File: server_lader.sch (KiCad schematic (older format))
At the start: 75 parts, among them IC1 ATMEGA168PA-A, IC2 DAC8560, P1 5V_Vbatt, P10 DISPLAY_STECKER, P11 on/off, P12 A_regulation_out, P2 DISPLAY_STECKER, P3 CONN_02X03, P4 I2C, P5 IP+, P6 IP-, P7 UART, P8 CONN_01X01, P9 Drehrad, U1 ACS758, U2 LTV-356T, U3 ADUM3441, U4 RD-0512D, U5 TPS7A4901, U6 OPA188, U7 LM4040, Y1 RESONATEUR

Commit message: bugfixes und Vormerkungen für nächsten Version
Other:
- note added: "Änderungen für nächste Version:\n-Kurzschlussbrücke für 5VRT und Power_GND vorsehen\n-abblockkondensatoren für Button vorsehen\n-alternative Bestückungsvariante mit anderem Stromsensor"
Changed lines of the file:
@@
 LIBS:contrib
 LIBS:valves
+LIBS:toni
 LIBS:server_lader-cache
 EELAYER 25 0
@@
 Text Notes 9200 4400 0    60   ~ 0
 RFB = 10k\nRG1 = 3,3k\nRG2 = 10k
+Text Notes 7850 5850 0    60   ~ 0
+Änderungen für nächste Version:\n-Kurzschlussbrücke für 5VRT und Power_GND vorsehen\n-abblockkondensatoren für Button vorsehen\n-alternative Bestückungsvariante mit anderem Stromsensor
 $EndSCHEMATC

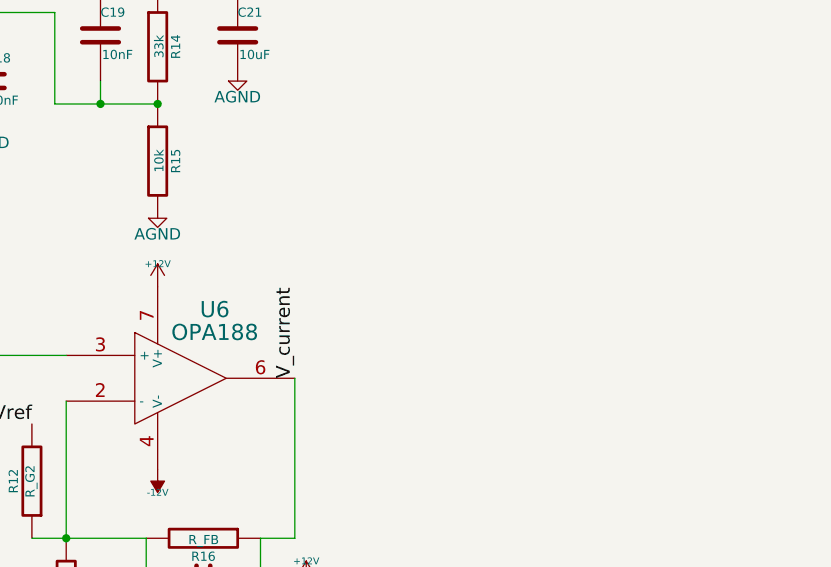
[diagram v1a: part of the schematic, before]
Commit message: Datenblätter und Schaltplananpassungen wegen neuem OPV im Ausgangszweig
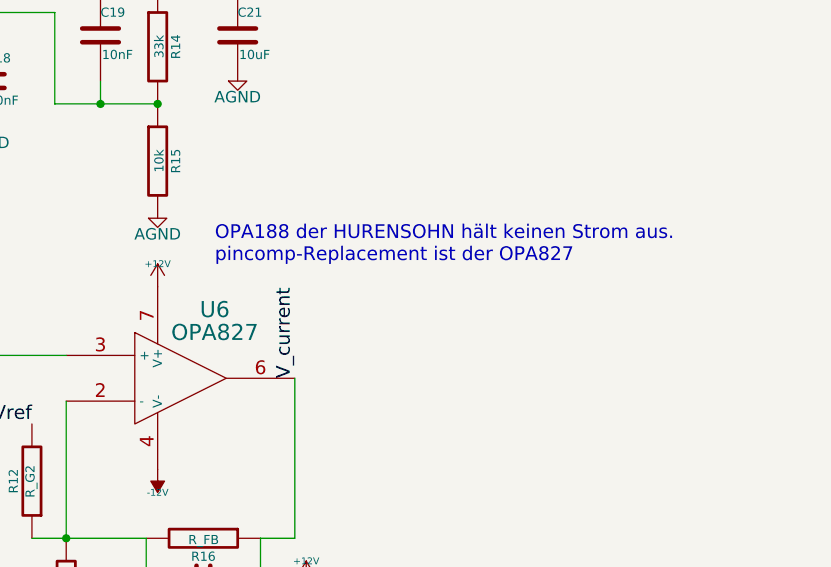
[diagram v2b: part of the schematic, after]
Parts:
- U6: value OPA188 -> OPA827
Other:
- note added: "OPA188 der HURENSOHN hält keinen Strom aus.\npincomp-Replacement ist der OPA827"
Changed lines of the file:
@@
 LIBS:contrib
 LIBS:valves
-LIBS:toni
 LIBS:server_lader-cache
 EELAYER 25 0
@@
 P 10450 3150
 F 0 "U6" H 10600 3450 70  0000 C CNN
-F 1 "OPA188" H 10600 3350 70  0000 C CNN
+F 1 "OPA827" H 10600 3350 70  0000 C CNN
 F 2 "SMD_Packages:SSOP-8" H 10450 3150 60  0001 C CNN
 F 3 "" H 10450 3150 60  0000 C CNN
@@
 Text Notes 7850 5850 0    60   ~ 0
 Änderungen für nächste Version:\n-Kurzschlussbrücke für 5VRT und Power_GND vorsehen\n-abblockkondensatoren für Button vorsehen\n-alternative Bestückungsvariante mit anderem Stromsensor
+Text Notes 10600 2650 0    60   ~ 0
+OPA188 der HURENSOHN hält keinen Strom aus.\npincomp-Replacement ist der OPA827
 $EndSCHEMATC

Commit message: kleine Änderungen
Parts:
- R2: value 200R -> 220R
- R4, R5: value 20k -> 22k
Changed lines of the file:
@@
 LIBS:contrib
 LIBS:valves
+LIBS:toni
 LIBS:server_lader-cache
 EELAYER 25 0
@@
 P 4000 1450
 F 0 "R4" V 4080 1450 40  0000 C CNN
-F 1 "20k" V 4007 1451 40  0000 C CNN
+F 1 "22k" V 4007 1451 40  0000 C CNN
 F 2 "SMD_Packages:SMD-0805" V 3930 1450 30  0001 C CNN
 F 3 "" H 4000 1450 30  0000 C CNN
@@
 P 4400 3500
 F 0 "R5" V 4480 3500 40  0000 C CNN
-F 1 "20k" V 4407 3501 40  0000 C CNN
+F 1 "22k" V 4407 3501 40  0000 C CNN
 F 2 "SMD_Packages:SMD-0805" V 4330 3500 30  0001 C CNN
 F 3 "" H 4400 3500 30  0000 C CNN
@@
 P 3850 1400
 F 0 "R2" V 3930 1400 40  0000 C CNN
-F 1 "200R" V 3857 1401 40  0000 C CNN
+F 1 "220R" V 3857 1401 40  0000 C CNN
 F 2 "SMD_Packages:SMD-0805" V 3780 1400 30  0001 C CNN
 F 3 "" H 3850 1400 30  0000 C CNN

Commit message: rescue_lib für schaltplan angelegt
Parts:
- C1, C10, C11, C12, C13, C14, C15, C16, C17, C18, C19, C2, C20, C21, C22, C23, C24, C25, C26, C27, C3, C4, C5, C6, C7, C8, C9: symbol C -> C-RESCUE-server_lader
- D1: symbol ZENER -> ZENER-RESCUE-server_lader
- D2: symbol LED -> LED-RESCUE-server_lader
- IC1: symbol ATMEGA168PA-A -> ATMEGA168PA-A-RESCUE-server_lader
- R1, R10, R11, R12, R13, R14, R15, R16, R17, R18, R19, R2, R20, R21, R3, R4, R5, R6, R7, R8, R9: symbol R -> R-RESCUE-server_lader
- U6: symbol TL071 -> TL071-RESCUE-server_lader
